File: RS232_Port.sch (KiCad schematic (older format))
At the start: 9 parts

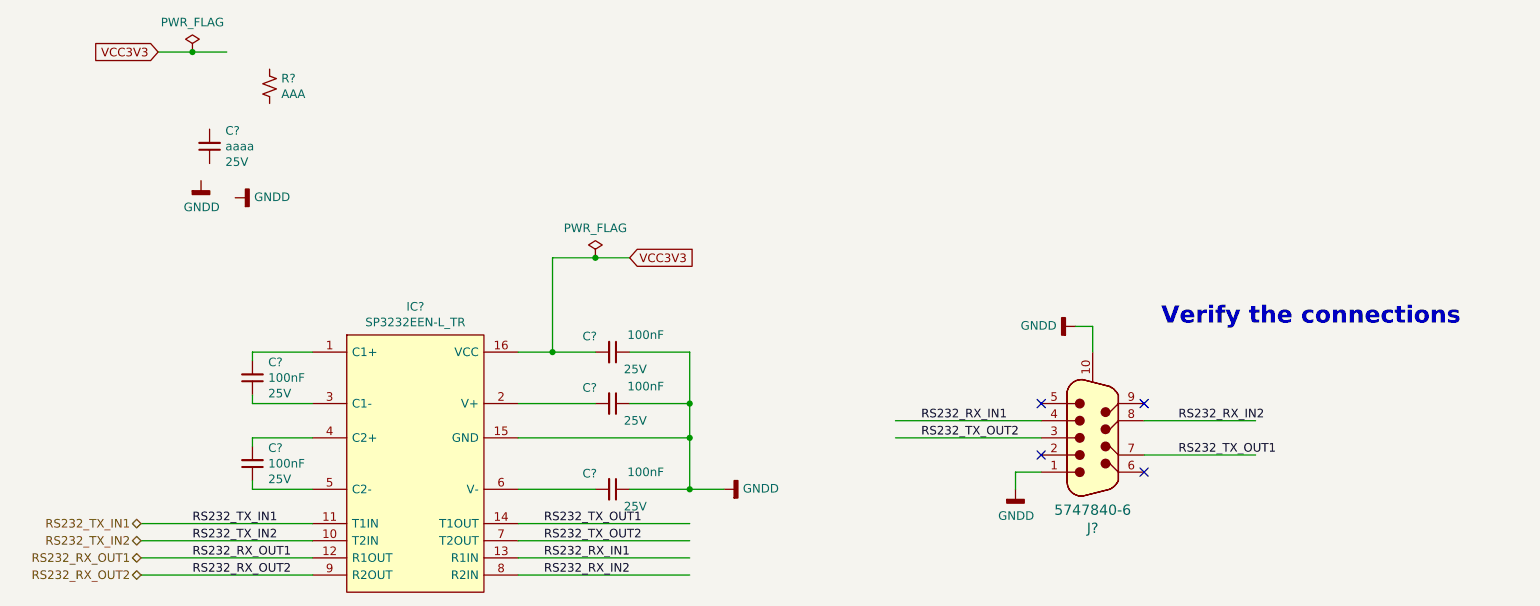
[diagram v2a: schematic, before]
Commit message: PCB created and schematics annotated High speed connections added to the BTB
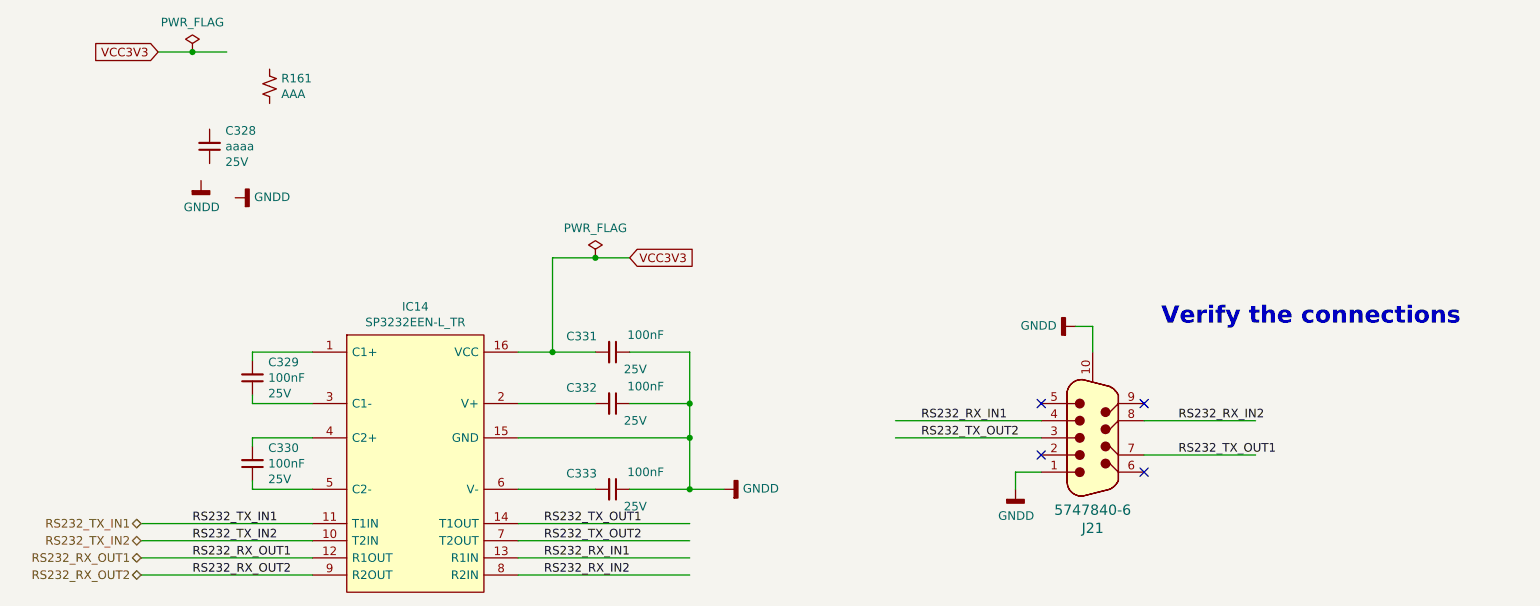
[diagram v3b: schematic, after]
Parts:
- gave numbers to parts that had none: 9
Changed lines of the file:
@@
 $EndDescr
 $Comp
-L GM_Interface_IC:SP3232EEN-L_TR IC?
+L GM_Interface_IC:SP3232EEN-L_TR IC14
 U 1 1 60397EEB
 P 3450 3150
-F 0 "IC?" H 3850 3315 50  0000 C CNN
+F 0 "IC14" H 3850 3315 50  0000 C CNN
 F 1 "SP3232EEN-L_TR" H 3850 3224 50  0000 C CNN
 F 2 "GM_SOIC:SOIC127P600X175-16N" H 5300 3450 50  0001 L CNN
@@
 $EndComp
 $Comp
-L dk_D-Sub-Connectors:5747840-3 J?
+L dk_D-Sub-Connectors:5747840-3 J21
 U 1 1 6039B1EE
 P 7800 3750
-F 0 "J?" H 7800 4277 60  0000 C CNN
+F 0 "J21" H 7800 4277 60  0000 C CNN
 F 1 "5747840-6" H 7800 4171 60  0000 C CNN
 F 2 "digikey-footprints:DSUB-9_Jack_5747840-3" H 8000 3950 60  0001 L CNN
@@
 P 2650 2050
 AR Path="/601E7C5A/603A1EC9" Ref="C?"  Part="1"
-AR Path="/60391560/603A1EC9" Ref="C?"  Part="1"
-F 0 "C?" H 2558 1959 50  0000 R CNN
+AR Path="/60391560/603A1EC9" Ref="C328"  Part="1"
+F 0 "C328" H 2558 1959 50  0000 R CNN
 F 1 "aaaa" H 2558 2050 50  0000 R CNN
 F 2 "Capacitor_SMD:C_0603_1608Metric_Pad1.08x0.95mm_HandSolder" H 2650 2050 50  0001 C CNN
@@
 AR Path="/601DF0A6/603A1ED1" Ref="#PWR?"  Part="1"
 AR Path="/601E7C5A/603A1ED1" Ref="#PWR?"  Part="1"
-AR Path="/60391560/603A1ED1" Ref="#PWR?"  Part="1"
-F 0 "#PWR?" H 2600 2000 50  0001 C CNN
+AR Path="/60391560/603A1ED1" Ref="#PWR0169"  Part="1"
+F 0 "#PWR0169" H 2600 2000 50  0001 C CNN
 F 1 "GNDD" H 2604 2095 50  0000 C CNN
 F 2 "" H 2600 2250 50  0001 C CNN
@@
 P 2550 1500
 AR Path="/601E7C5A/603A1EDB" Ref="#FLG?"  Part="1"
-AR Path="/60391560/603A1EDB" Ref="#FLG?"  Part="1"
-F 0 "#FLG?" H 2550 1575 50  0001 C CNN
+AR Path="/60391560/603A1EDB" Ref="#FLG055"  Part="1"
+F 0 "#FLG055" H 2550 1575 50  0001 C CNN
 F 1 "PWR_FLAG" H 2550 1673 50  0000 C CNN
 F 2 "" H 2550 1500 50  0001 C CNN
@@
 AR Path="/601E7B38/603B0E41" Ref="R?"  Part="1"
 AR Path="/601E7BF0/603B0E41" Ref="R?"  Part="1"
-AR Path="/60391560/603B0E41" Ref="R?"  Part="1"
-F 0 "R?" H 3068 1746 50  0000 L CNN
+AR Path="/60391560/603B0E41" Ref="R161"  Part="1"
+F 0 "R161" H 3068 1746 50  0000 L CNN
 F 1 "AAA" H 3068 1655 50  0000 L CNN
 F 2 "Resistor_SMD:R_0603_1608Metric_Pad0.98x0.95mm_HandSolder" H 3000 1700 50  0001 C CNN
@@
 P 5000 3250
 AR Path="/601E7C5A/603B7383" Ref="C?"  Part="1"
-AR Path="/60391560/603B7383" Ref="C?"  Part="1"
-F 0 "C?" V 4908 3159 50  0000 R CNN
+AR Path="/60391560/603B7383" Ref="C331"  Part="1"
+F 0 "C331" V 4908 3159 50  0000 R CNN
 F 1 "100nF" V 4900 3550 50  0000 R CNN
 F 2 "Capacitor_SMD:C_0603_1608Metric_Pad1.08x0.95mm_HandSolder" H 5000 3250 50  0001 C CNN
@@
 P 5000 3550
 AR Path="/601E7C5A/603BA37E" Ref="C?"  Part="1"
-AR Path="/60391560/603BA37E" Ref="C?"  Part="1"
-F 0 "C?" V 4908 3459 50  0000 R CNN
+AR Path="/60391560/603BA37E" Ref="C332"  Part="1"
+F 0 "C332" V 4908 3459 50  0000 R CNN
 F 1 "100nF" V 4900 3850 50  0000 R CNN
 F 2 "Capacitor_SMD:C_0603_1608Metric_Pad1.08x0.95mm_HandSolder" H 5000 3550 50  0001 C CNN
@@
 P 5000 4050
 AR Path="/601E7C5A/603BA4F4" Ref="C?"  Part="1"
-AR Path="/60391560/603BA4F4" Ref="C?"  Part="1"
-F 0 "C?" V 4908 3959 50  0000 R CNN
+AR Path="/60391560/603BA4F4" Ref="C333"  Part="1"
+F 0 "C333" V 4908 3959 50  0000 R CNN
 F 1 "100nF" V 4900 4350 50  0000 R CNN
 F 2 "Capacitor_SMD:C_0603_1608Metric_Pad1.08x0.95mm_HandSolder" H 5000 4050 50  0001 C CNN
@@
 Connection ~ 5450 3750
 $Comp
-L power:GNDD #PWR?
+L power:GNDD #PWR0171
 U 1 1 603C1885
 P 5650 4050
-F 0 "#PWR?" H 5650 3800 50  0001 C CNN
+F 0 "#PWR0171" H 5650 3800 50  0001 C CNN
 F 1 "GNDD" V 5654 3940 50  0000 R CNN
 F 2 "" H 5650 4050 50  0001 C CNN
@@
 $EndComp
 $Comp
-L power:GNDD #PWR?
+L power:GNDD #PWR0170
 U 1 1 603C229B
 P 2800 2350
-F 0 "#PWR?" H 2800 2100 50  0001 C CNN
+F 0 "#PWR0170" H 2800 2100 50  0001 C CNN
 F 1 "GNDD" V 2804 2240 50  0000 R CNN
 F 2 "" H 2800 2350 50  0001 C CNN
@@
 P 4900 2700
 AR Path="/601E7C5A/603DB67B" Ref="#FLG?"  Part="1"
-AR Path="/60391560/603DB67B" Ref="#FLG?"  Part="1"
-F 0 "#FLG?" H 4900 2775 50  0001 C CNN
+AR Path="/60391560/603DB67B" Ref="#FLG056"  Part="1"
+F 0 "#FLG056" H 4900 2775 50  0001 C CNN
 F 1 "PWR_FLAG" H 4900 2873 50  0000 C CNN
 F 2 "" H 4900 2700 50  0001 C CNN
@@
 AR Path="/601DF0A6/603DEA45" Ref="#PWR?"  Part="1"
 AR Path="/601E7C5A/603DEA45" Ref="#PWR?"  Part="1"
-AR Path="/60391560/603DEA45" Ref="#PWR?"  Part="1"
-F 0 "#PWR?" H 7350 3800 50  0001 C CNN
+AR Path="/60391560/603DEA45" Ref="#PWR0172"  Part="1"
+F 0 "#PWR0172" H 7350 3800 50  0001 C CNN
 F 1 "GNDD" H 7354 3895 50  0000 C CNN
 F 2 "" H 7350 4050 50  0001 C CNN
@@
 P 2900 3400
 AR Path="/601E7C5A/603E884E" Ref="C?"  Part="1"
-AR Path="/60391560/603E884E" Ref="C?"  Part="1"
-F 0 "C?" H 2808 3309 50  0000 R CNN
+AR Path="/60391560/603E884E" Ref="C329"  Part="1"
+F 0 "C329" H 2808 3309 50  0000 R CNN
 F 1 "100nF" H 2808 3400 50  0000 R CNN
 F 2 "Capacitor_SMD:C_0603_1608Metric_Pad1.08x0.95mm_HandSolder" H 2900 3400 50  0001 C CNN
@@
 P 2900 3900
 AR Path="/601E7C5A/603E9129" Ref="C?"  Part="1"
-AR Path="/60391560/603E9129" Ref="C?"  Part="1"
-F 0 "C?" H 2808 3809 50  0000 R CNN
+AR Path="/60391560/603E9129" Ref="C330"  Part="1"
+F 0 "C330" H 2808 3809 50  0000 R CNN
 F 1 "100nF" H 2808 3900 50  0000 R CNN
 F 2 "Capacitor_SMD:C_0603_1608Metric_Pad1.08x0.95mm_HandSolder" H 2900 3900 50  0001 C CNN
@@
 Verify the connections
 $Comp
-L power:GNDD #PWR?
+L power:GNDD #PWR0173
 U 1 1 6041AC3C
 P 7700 3100
-F 0 "#PWR?" H 7700 2850 50  0001 C CNN
+F 0 "#PWR0173" H 7700 2850 50  0001 C CNN
 F 1 "GNDD" V 7704 2990 50  0000 R CNN
 F 2 "" H 7700 3100 50  0001 C CNN

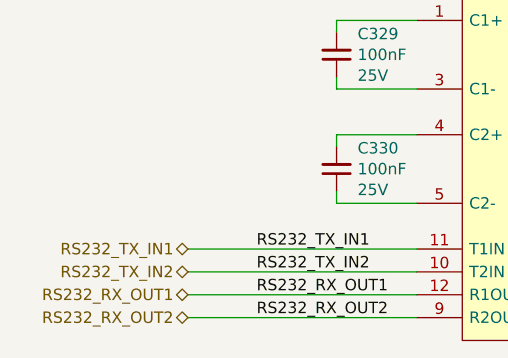
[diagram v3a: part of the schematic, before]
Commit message: Connections were made to FPGA banks
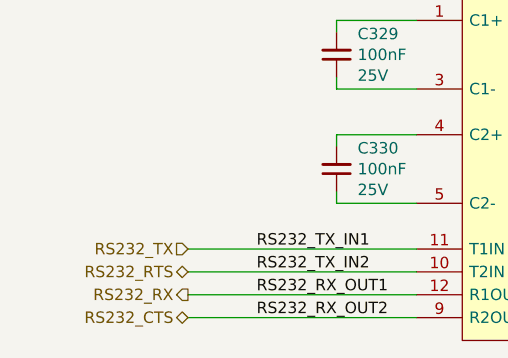
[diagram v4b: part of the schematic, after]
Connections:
- net labels added: RS232_CTS, RS232_RTS, RS232_RX, RS232_TX
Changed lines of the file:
@@
 $Descr A4 11693 8268
 encoding utf-8
-Sheet 20 25
+Sheet 25 25
 Title ""
 Date ""
@@
 Text Label 2550 4550 0    50   ~ 0
 RS232_RX_OUT2
-Text HLabel 2250 4250 0    50   BiDi ~ 0
-RS232_TX_IN1
+Text HLabel 2250 4250 0    50   Input ~ 0
+RS232_TX
 Text HLabel 2250 4350 0    50   BiDi ~ 0
-RS232_TX_IN2
-Text HLabel 2250 4450 0    50   BiDi ~ 0
-RS232_RX_OUT1
+RS232_RTS
+Text HLabel 2250 4450 0    50   Output ~ 0
+RS232_RX
 Text HLabel 2250 4550 0    50   BiDi ~ 0
-RS232_RX_OUT2
+RS232_CTS
 Text Label 4600 4250 0    50   ~ 0
 RS232_TX_OUT1

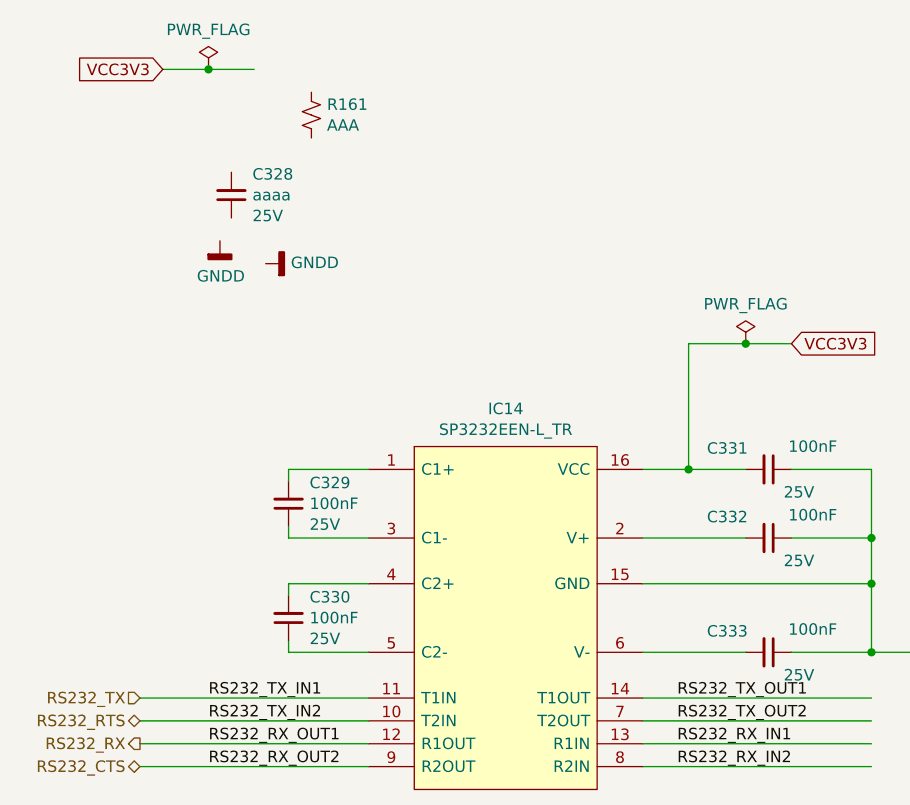
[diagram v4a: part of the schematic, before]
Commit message: Corrected PCB import errors
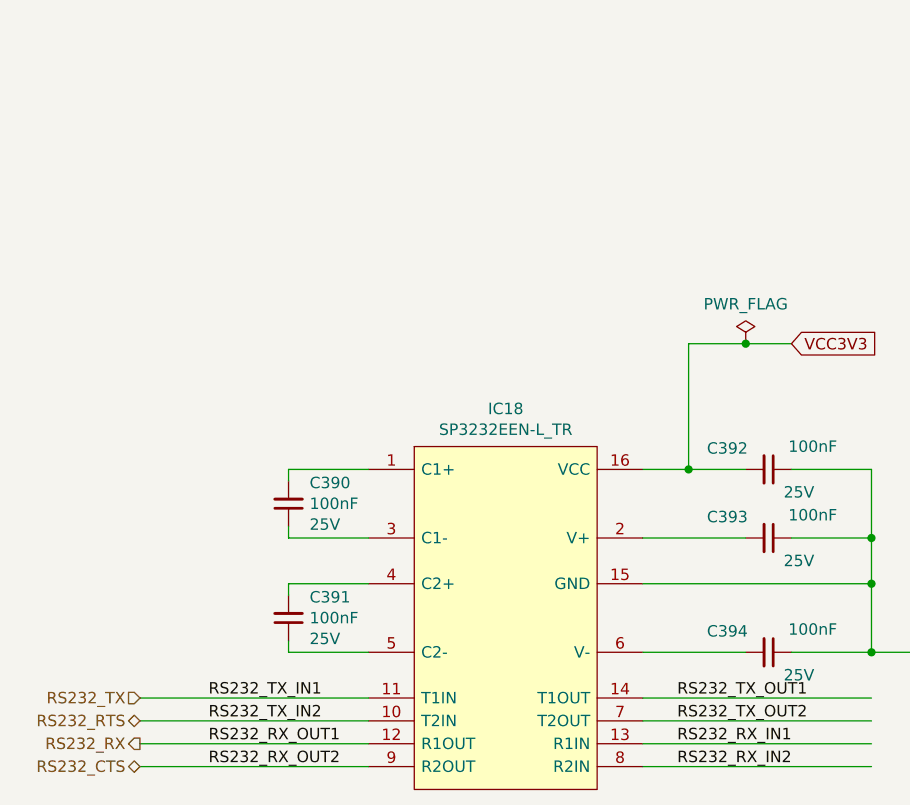
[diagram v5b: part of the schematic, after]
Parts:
- removed C328: aaaa, Capacitor_SMD:C_0603_1608Metric_Pad1.08x0.95mm_HandSolder, symbol Device:C_Small
- removed R161: AAA, Resistor_SMD:R_0603_1608Metric_Pad0.98x0.95mm_HandSolder, symbol Device:R_Small_US
- renumbered C329 to C390, C330 to C391, C331 to C392, C332 to C393, C333 to C394, IC14 to IC18
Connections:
- wire segments 41 -> 39
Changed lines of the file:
@@
 $EndDescr
 $Comp
-L GM_Interface_IC:SP3232EEN-L_TR IC14
+L GM_Interface_IC:SP3232EEN-L_TR IC18
 U 1 1 60397EEB
 P 3450 3150
-F 0 "IC14" H 3850 3315 50  0000 C CNN
+F 0 "IC18" H 3850 3315 50  0000 C CNN
 F 1 "SP3232EEN-L_TR" H 3850 3224 50  0000 C CNN
 F 2 "GM_SOIC:SOIC127P600X175-16N" H 5300 3450 50  0001 L CNN
@@
 $Comp
 L Device:C_Small C?
-U 1 1 603A1EC9
-P 2650 2050
-AR Path="/601E7C5A/603A1EC9" Ref="C?"  Part="1"
-AR Path="/60391560/603A1EC9" Ref="C328"  Part="1"
-F 0 "C328" H 2558 1959 50  0000 R CNN
-F 1 "aaaa" H 2558 2050 50  0000 R CNN
-F 2 "Capacitor_SMD:C_0603_1608Metric_Pad1.08x0.95mm_HandSolder" H 2650 2050 50  0001 C CNN
-F 3 "~" H 2650 2050 50  0001 C CNN
-F 4 "25V" H 2558 2141 50  0000 R CNN "Voltage"
-	1    2650 2050
-	-1   0    0    1
-$EndComp
-$Comp
-L power:GNDD #PWR?
-U 1 1 603A1ED1
-P 2600 2250
-AR Path="/601DF0A6/603A1ED1" Ref="#PWR?"  Part="1"
-AR Path="/601E7C5A/603A1ED1" Ref="#PWR?"  Part="1"
-AR Path="/60391560/603A1ED1" Ref="#PWR0169"  Part="1"
-F 0 "#PWR0169" H 2600 2000 50  0001 C CNN
-F 1 "GNDD" H 2604 2095 50  0000 C CNN
-F 2 "" H 2600 2250 50  0001 C CNN
-F 3 "" H 2600 2250 50  0001 C CNN
-	1    2600 2250
-	1    0    0    -1
-$EndComp
-Text GLabel 2350 1500 0    50   Input ~ 0
-VCC3V3
-$Comp
-L power:PWR_FLAG #FLG?
-U 1 1 603A1EDB
-P 2550 1500
-AR Path="/601E7C5A/603A1EDB" Ref="#FLG?"  Part="1"
-AR Path="/60391560/603A1EDB" Ref="#FLG055"  Part="1"
-F 0 "#FLG055" H 2550 1575 50  0001 C CNN
-F 1 "PWR_FLAG" H 2550 1673 50  0000 C CNN
-F 2 "" H 2550 1500 50  0001 C CNN
-F 3 "~" H 2550 1500 50  0001 C CNN
-	1    2550 1500
-	1    0    0    -1
-$EndComp
-Connection ~ 2550 1500
-Wire Wire Line
-	2550 1500 2750 1500
-Wire Wire Line
-	2350 1500 2550 1500
-$Comp
-L Device:R_Small_US R?
-U 1 1 603B0E41
-P 3000 1700
-AR Path="/601E7C5A/603B0E41" Ref="R?"  Part="1"
-AR Path="/601E7CC8/603B0E41" Ref="R?"  Part="1"
-AR Path="/601E7C92/603B0E41" Ref="R?"  Part="1"
-AR Path="/601E7C92/60257FE5/603B0E41" Ref="R?"  Part="1"
-AR Path="/601E7B38/603B0E41" Ref="R?"  Part="1"
-AR Path="/601E7BF0/603B0E41" Ref="R?"  Part="1"
-AR Path="/60391560/603B0E41" Ref="R161"  Part="1"
-F 0 "R161" H 3068 1746 50  0000 L CNN
-F 1 "AAA" H 3068 1655 50  0000 L CNN
-F 2 "Resistor_SMD:R_0603_1608Metric_Pad0.98x0.95mm_HandSolder" H 3000 1700 50  0001 C CNN
-F 3 "~" H 3000 1700 50  0001 C CNN
-	1    3000 1700
-	1    0    0    -1
-$EndComp
-$Comp
-L Device:C_Small C?
 U 1 1 603B7383
 P 5000 3250
 AR Path="/601E7C5A/603B7383" Ref="C?"  Part="1"
-AR Path="/60391560/603B7383" Ref="C331"  Part="1"
-F 0 "C331" V 4908 3159 50  0000 R CNN
+AR Path="/60391560/603B7383" Ref="C392"  Part="1"
+F 0 "C392" V 4908 3159 50  0000 R CNN
 F 1 "100nF" V 4900 3550 50  0000 R CNN
 F 2 "Capacitor_SMD:C_0603_1608Metric_Pad1.08x0.95mm_HandSolder" H 5000 3250 50  0001 C CNN
@@
 P 5000 3550
 AR Path="/601E7C5A/603BA37E" Ref="C?"  Part="1"
-AR Path="/60391560/603BA37E" Ref="C332"  Part="1"
-F 0 "C332" V 4908 3459 50  0000 R CNN
+AR Path="/60391560/603BA37E" Ref="C393"  Part="1"
+F 0 "C393" V 4908 3459 50  0000 R CNN
 F 1 "100nF" V 4900 3850 50  0000 R CNN
 F 2 "Capacitor_SMD:C_0603_1608Metric_Pad1.08x0.95mm_HandSolder" H 5000 3550 50  0001 C CNN
@@
 P 5000 4050
 AR Path="/601E7C5A/603BA4F4" Ref="C?"  Part="1"
-AR Path="/60391560/603BA4F4" Ref="C333"  Part="1"
-F 0 "C333" V 4908 3959 50  0000 R CNN
+AR Path="/60391560/603BA4F4" Ref="C394"  Part="1"
+F 0 "C394" V 4908 3959 50  0000 R CNN
 F 1 "100nF" V 4900 4350 50  0000 R CNN
 F 2 "Capacitor_SMD:C_0603_1608Metric_Pad1.08x0.95mm_HandSolder" H 5000 4050 50  0001 C CNN
@@
 Connection ~ 5450 3750
 $Comp
-L power:GNDD #PWR0171
+L power:GNDD #PWR0201
 U 1 1 603C1885
 P 5650 4050
-F 0 "#PWR0171" H 5650 3800 50  0001 C CNN
+F 0 "#PWR0201" H 5650 3800 50  0001 C CNN
 F 1 "GNDD" V 5654 3940 50  0000 R CNN
 F 2 "" H 5650 4050 50  0001 C CNN
@@
 	0    -1   -1   0
 $EndComp
-$Comp
-L power:GNDD #PWR0170
-U 1 1 603C229B
-P 2800 2350
-F 0 "#PWR0170" H 2800 2100 50  0001 C CNN
-F 1 "GNDD" V 2804 2240 50  0000 R CNN
-F 2 "" H 2800 2350 50  0001 C CNN
-F 3 "" H 2800 2350 50  0001 C CNN
-	1    2800 2350
-	0    -1   -1   0
-$EndComp
 Wire Wire Line
 	5650 4050 5450 4050
@@
 P 4900 2700
 AR Path="/601E7C5A/603DB67B" Ref="#FLG?"  Part="1"
-AR Path="/60391560/603DB67B" Ref="#FLG056"  Part="1"
-F 0 "#FLG056" H 4900 2775 50  0001 C CNN
+AR Path="/60391560/603DB67B" Ref="#FLG074"  Part="1"
+F 0 "#FLG074" H 4900 2775 50  0001 C CNN
 F 1 "PWR_FLAG" H 4900 2873 50  0000 C CNN
 F 2 "" H 4900 2700 50  0001 C CNN
@@
 AR Path="/601DF0A6/603DEA45" Ref="#PWR?"  Part="1"
 AR Path="/601E7C5A/603DEA45" Ref="#PWR?"  Part="1"
-AR Path="/60391560/603DEA45" Ref="#PWR0172"  Part="1"
-F 0 "#PWR0172" H 7350 3800 50  0001 C CNN
+AR Path="/60391560/603DEA45" Ref="#PWR0202"  Part="1"
+F 0 "#PWR0202" H 7350 3800 50  0001 C CNN
 F 1 "GNDD" H 7354 3895 50  0000 C CNN
 F 2 "" H 7350 4050 50  0001 C CNN
@@
 P 2900 3400
 AR Path="/601E7C5A/603E884E" Ref="C?"  Part="1"
-AR Path="/60391560/603E884E" Ref="C329"  Part="1"
-F 0 "C329" H 2808 3309 50  0000 R CNN
+AR Path="/60391560/603E884E" Ref="C390"  Part="1"
+F 0 "C390" H 2808 3309 50  0000 R CNN
 F 1 "100nF" H 2808 3400 50  0000 R CNN
 F 2 "Capacitor_SMD:C_0603_1608Metric_Pad1.08x0.95mm_HandSolder" H 2900 3400 50  0001 C CNN
@@
 P 2900 3900
 AR Path="/601E7C5A/603E9129" Ref="C?"  Part="1"
-AR Path="/60391560/603E9129" Ref="C330"  Part="1"
-F 0 "C330" H 2808 3809 50  0000 R CNN
+AR Path="/60391560/603E9129" Ref="C391"  Part="1"
+F 0 "C391" H 2808 3809 50  0000 R CNN
 F 1 "100nF" H 2808 3900 50  0000 R CNN
 F 2 "Capacitor_SMD:C_0603_1608Metric_Pad1.08x0.95mm_HandSolder" H 2900 3900 50  0001 C CNN
@@
 Verify the connections
 $Comp
-L power:GNDD #PWR0173
+L power:GNDD #PWR0203
 U 1 1 6041AC3C
 P 7700 3100
-F 0 "#PWR0173" H 7700 2850 50  0001 C CNN
+F 0 "#PWR0203" H 7700 2850 50  0001 C CNN
 F 1 "GNDD" V 7704 2990 50  0000 R CNN
 F 2 "" H 7700 3100 50  0001 C CNN
